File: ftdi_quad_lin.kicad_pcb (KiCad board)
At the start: 2 copper layers, 54.2 x 53 mm, 95 parts, among them J1 USB_C_Receptacle_USB2.0_16P, J2 Screw_Terminal_01x03, J3 Screw_Terminal_01x03, J4 Screw_Terminal_01x03, J5 Screw_Terminal_01x03, J6 Conn_01x10, J8 Barrel_Jack_MountingPin, U1 FT4232H, U2 TJA1029T, U3 AP2112K-3.3, U4 93CxxB, U5 TJA1029T, U6 TJA1029T, U7 TJA1029T, U8 74HC595, Y1 12Mhz

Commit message: reoredered
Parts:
- moved C1 4.00 mm to (92.2, 104.0)
- moved C3 2.99 mm to (95.8, 103.5), turned to 180 degrees
- moved R4 2.85 mm to (89.0, 102.8), turned to 180 degrees
- moved C7 1.10 mm to (92.2, 98.7)
- moved FB2 0.90 mm to (88.5, 100.2), turned to 0 degrees
- moved R3 0.25 mm to (95.8, 105.5)
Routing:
- net GND: track 148.0 -> 137.6 mm, vias 65 -> 79
- net Net-(U1-VPHY): track 17.2 -> 11.5 mm
- net Net-(J1-CC1): track 3.45 -> 6.47 mm
- net Net-(U1-OSCO): track 8.19 -> 9.53 mm
- net +3V3: track 84.4 -> 85.7 mm

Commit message: Using bus
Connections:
- net /EECLK renamed /eeprom/EECLK
- net /EECS renamed /eeprom/EECS
- net /EEDATA renamed /eeprom/EEDATA
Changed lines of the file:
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@@
 	(net 61 "unconnected-(Y1-Pad2)")
 	(net 62 "unconnected-(Y1-Pad4)")
-	(net 63 "/EECS")
-	(net 64 "/EECLK")
-	(net 65 "/EEDATA")
+	(net 63 "/eeprom/EECS")
+	(net 64 "/eeprom/EECLK")
+	(net 65 "/eeprom/EEDATA")
 	(net 66 "Net-(U8-QB)")
 	(net 67 "/PWREN")
@@
 		)
 		(property ki_fp_filters "C_*")
-		(sheetname "Root")
-		(sheetfile "ftdi_quad_lin.kicad_sch")
+		(sheetname "eeprom")
+		(sheetfile "eeprom.kicad_sch")
 		(attr smd)
 		(fp_line
@@
 		)
 		(property ki_fp_filters "DIP*W7.62mm* SOIC*3.9x9.9mm*P1.27mm* TSSOP*4.4x5mm*P0.65mm* SOIC*5.3x10.2mm*P1.27mm* SOIC*7.5x10.3mm*P1.27mm*")
-		(sheetname "Root")
-		(sheetfile "ftdi_quad_lin.kicad_sch")
+		(sheetname "leds_indication")
+		(sheetfile "leds_indication.kicad_sch")
 		(attr smd)
 		(fp_line
@@
 			(layers "F.Cu" "F.Paste" "F.Mask")
 			(roundrect_rratio 0.25)
-			(net 64 "/EECLK")
+			(net 64 "/eeprom/EECLK")
 			(pinfunction "SRCLK")
 			(pintype "input")
@@
 			(layers "F.Cu" "F.Paste" "F.Mask")
 			(roundrect_rratio 0.25)
-			(net 63 "/EECS")
+			(net 63 "/eeprom/EECS")
 			(pinfunction "RCLK")
 			(pintype "input")
@@
 			(layers "F.Cu" "F.Paste" "F.Mask")
 			(roundrect_rratio 0.25)
-			(net 65 "/EEDATA")
+			(net 65 "/eeprom/EEDATA")
 			(pinfunction "SER")
 			(pintype "input")
@@
 		)
 		(property ki_fp_filters "R_*")
-		(sheetname "Root")
-		(sheetfile "ftdi_quad_lin.kicad_sch")
+		(sheetname "eeprom")
+		(sheetfile "eeprom.kicad_sch")
 		(attr smd)
 		(fp_line
@@
 			(layers "F.Cu" "F.Paste" "F.Mask")
 			(roundrect_rratio 0.243902)
-			(net 63 "/EECS")
+			(net 63 "/eeprom/EECS")
 			(pintype "passive")
 		)
@@
 		(tags "capacitor handsolder")
 		(property "Reference" "C1"
-			(at -3.1875 0 360)
+			(at -3.1875 0 0)
 			(layer "F.SilkS")
 			(effects
@@
 		)
 		(fp_text user "${REFERENCE}"
-			(at 0 0 360)
+			(at 0 0 0)
 			(layer "F.Fab")
 			(effects
@@
 		)
 		(property ki_fp_filters "R_*")
-		(sheetname "Root")
-		(sheetfile "ftdi_quad_lin.kicad_sch")
+		(sheetname "leds_indication")
+		(sheetfile "leds_indication.kicad_sch")
 		(attr smd)
 		(fp_line
@@
 			(layers "F.Cu" "F.Paste" "F.Mask")
 			(roundrect_rratio 0.25)
-			(net 65 "/EEDATA")
+			(net 65 "/eeprom/EEDATA")
 			(pinfunction "EEDATA")
 			(pintype "bidirectional")
@@
 			(layers "F.Cu" "F.Paste" "F.Mask")
 			(roundrect_rratio 0.25)
-			(net 64 "/EECLK")
+			(net 64 "/eeprom/EECLK")
 			(pinfunction "EECLK")
 			(pintype "output")
@@
 			(layers "F.Cu" "F.Paste" "F.Mask")
 			(roundrect_rratio 0.25)
-			(net 63 "/EECS")
+			(net 63 "/eeprom/EECS")
 			(pinfunction "EECS")
 			(pintype "output")
@@
 		)
 		(property ki_fp_filters "DIP*W7.62mm* SOIC*3.9x4.9mm*")
-		(sheetname "Root")
-		(sheetfile "ftdi_quad_lin.kicad_sch")
+		(sheetname "eeprom")
+		(sheetfile "eeprom.kicad_sch")
 		(attr smd)
 		(fp_line
@@
 			(layers "F.Cu" "F.Paste" "F.Mask")
 			(roundrect_rratio 0.25)
-			(net 63 "/EECS")
+			(net 63 "/eeprom/EECS")
 			(pinfunction "CS")
 			(pintype "input")
@@
 			(layers "F.Cu" "F.Paste" "F.Mask")
 			(roundrect_rratio 0.25)
-			(net 64 "/EECLK")
+			(net 64 "/eeprom/EECLK")
 			(pinfunction "SCLK")
 			(pintype "input")
@@
 			(layers "F.Cu" "F.Paste" "F.Mask")
 			(roundrect_rratio 0.25)
-			(net 65 "/EEDATA")
+			(net 65 "/eeprom/EEDATA")
 			(pinfunction "DI")
 			(pintype "input")
@@
 		)
 		(property ki_fp_filters "C_*")
-		(sheetname "Root")
-		(sheetfile "ftdi_quad_lin.kicad_sch")
+		(sheetname "leds_indication")
+		(sheetfile "leds_indication.kicad_sch")
 		(attr smd)
 		(fp_line
@@
 		)
 		(property ki_fp_filters "R_*")
-		(sheetname "Root")
-		(sheetfile "ftdi_quad_lin.kicad_sch")
+		(sheetname "leds_indication")
+		(sheetfile "leds_indication.kicad_sch")
 		(attr smd)
 		(fp_line
@@
 		)
 		(property ki_fp_filters "R_*")
-		(sheetname "Root")
-		(sheetfile "ftdi_quad_lin.kicad_sch")
+		(sheetname "eeprom")
+		(sheetfile "eeprom.kicad_sch")
 		(attr smd)
 		(fp_line
@@
 			(layers "F.Cu" "F.Paste" "F.Mask")
 			(roundrect_rratio 0.243902)
-			(net 64 "/EECLK")
+			(net 64 "/eeprom/EECLK")
 			(pintype "passive")
 		)
@@
 		)
 		(property ki_fp_filters "R_*")
-		(sheetname "Root")
-		(sheetfile "ftdi_quad_lin.kicad_sch")
+		(sheetname "leds_indication")
+		(sheetfile "leds_indication.kicad_sch")
 		(attr smd)
 		(fp_line
@@
 			)
 		)
-		(sheetname "Root")
-		(sheetfile "ftdi_quad_lin.kicad_sch")
+		(sheetname "leds_indication")
+		(sheetfile "leds_indication.kicad_sch")
 		(attr smd)
 		(fp_line
@@
 		)
 		(property ki_fp_filters "R_*")
-		(sheetname "Root")
-		(sheetfile "ftdi_quad_lin.kicad_sch")
+		(sheetname "leds_indication")
+		(sheetfile "leds_indication.kicad_sch")
 		(attr smd)
 		(fp_line
@@
 		)
 		(property "Value" "5.1k"
-			(at 0 1.65 360)
+			(at 0 1.65 0)
 			(layer "F.Fab")
 			(effects
@@
 		)
 		(fp_text user "${REFERENCE}"
-			(at 0 0 360)
+			(at 0 0 0)
 			(layer "F.Fab")
 			(effects
@@
 		)
 		(property ki_fp_filters "R_*")
-		(sheetname "Root")
-		(sheetfile "ftdi_quad_lin.kicad_sch")
+		(sheetname "leds_indication")
+		(sheetfile "leds_indication.kicad_sch")
 		(attr smd)
 		(fp_line
@@
 		)
 		(property ki_fp_filters "R_*")
-		(sheetname "Root")
-		(sheetfile "ftdi_quad_lin.kicad_sch")
+		(sheetname "eeprom")
+		(sheetfile "eeprom.kicad_sch")
 		(attr smd)
 		(fp_line
@@
 		)
 		(property ki_fp_filters "R_*")
-		(sheetname "Root")
-		(sheetfile "ftdi_quad_lin.kicad_sch")
+		(sheetname "eeprom")
+		(sheetfile "eeprom.kicad_sch")
 		(attr smd)
 		(fp_line
@@
 			(layers "F.Cu" "F.Paste" "F.Mask")
 			(roundrect_rratio 0.243902)
-			(net 65 "/EEDATA")
+			(net 65 "/eeprom/EEDATA")
 			(pintype "passive")
 		)
@@
 		(tags "inductor handsolder")
 		(property "Reference" "FB2"
-			(at 0 -1.43 360)
+			(at 0 -1.43 0)
 			(layer "F.SilkS")
 			(effects
@@
 		)
 		(property "Value" "600R/0.5A"
-			(at -1.25 1.93 360)
+			(at -1.25 1.93 0)
 			(layer "F.Fab")
 			(effects
@@
 		)
 		(fp_text user "${REFERENCE}"
-			(at 0 0 360)
+			(at 0 0 0)
 			(layer "F.Fab")
 			(effects

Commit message: progress
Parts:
- added C30: 220n, Capacitor_SMD:C_0805_2012Metric_Pad1.18x1.45mm_HandSolder, F.Cu at (210.4, 9.20)
- added C31: 100n, Capacitor_SMD:C_0805_2012Metric_Pad1.18x1.45mm_HandSolder, F.Cu at (197.2, 10.6)
- added C32: 220n, Capacitor_SMD:C_0805_2012Metric_Pad1.18x1.45mm_HandSolder, F.Cu at (212.3, 30.8)
- added C33: 100n, Capacitor_SMD:C_0805_2012Metric_Pad1.18x1.45mm_HandSolder, F.Cu at (199.1, 32.2)
- added C34: 220n, Capacitor_SMD:C_0805_2012Metric_Pad1.18x1.45mm_HandSolder, F.Cu at (190.6, 31.1)
- added C35: 100n, Capacitor_SMD:C_0805_2012Metric_Pad1.18x1.45mm_HandSolder, F.Cu at (177.4, 32.5)
- added C36: 220n, Capacitor_SMD:C_0805_2012Metric_Pad1.18x1.45mm_HandSolder, F.Cu at (212.9, 47.6)
- added C37: 100n, Capacitor_SMD:C_0805_2012Metric_Pad1.18x1.45mm_HandSolder, F.Cu at (199.7, 49.0)
- added D11: 1N4148W, Diode_SMD:D_SOD-323_HandSoldering, F.Cu at (199.8, 13.6)
- added D12: 1N4148W, Diode_SMD:D_SOD-323_HandSoldering, F.Cu at (201.7, 35.2)
- added D13: 1N4148W, Diode_SMD:D_SOD-323_HandSoldering, F.Cu at (202.2, 52.0)
- added Q1: MMBT2222A, Package_TO_SOT_SMD:SOT-23, F.Cu at (200.1, 8.74)
- added Q10: MMBT2222A, Package_TO_SOT_SMD:SOT-23, F.Cu at (202.6, 47.1)
- added Q11: MMBT2222A, Package_TO_SOT_SMD:SOT-23, F.Cu at (209.9, 47.8)
- added Q12: MMBT2222A, Package_TO_SOT_SMD:SOT-23, F.Cu at (209.9, 51.4)
- added Q2: MMBT2222A, Package_TO_SOT_SMD:SOT-23, F.Cu at (207.4, 9.40)
- added Q3: MMBT2222A, Package_TO_SOT_SMD:SOT-23, F.Cu at (207.4, 12.9)
- added Q4: MMBT2222A, Package_TO_SOT_SMD:SOT-23, F.Cu at (201.9, 30.3)
- added Q5: MMBT2222A, Package_TO_SOT_SMD:SOT-23, F.Cu at (209.3, 31.0)
- added Q6: MMBT2222A, Package_TO_SOT_SMD:SOT-23, F.Cu at (209.3, 34.5)
- added Q7: MMBT2222A, Package_TO_SOT_SMD:SOT-23, F.Cu at (180.2, 30.6)
- added Q8: MMBT2222A, Package_TO_SOT_SMD:SOT-23, F.Cu at (187.6, 31.2)
- added Q9: MMBT2222A, Package_TO_SOT_SMD:SOT-23, F.Cu at (187.6, 34.8)
- added R26: 10k, Resistor_SMD:R_0805_2012Metric, F.Cu at (210.4, 12.9)
- added R27: 10k, Resistor_SMD:R_0805_2012Metric, F.Cu at (200.1, 11.6)
- added R28: 10k, Resistor_SMD:R_0805_2012Metric, F.Cu at (205.5, 31.4)
- added R29: 330k, Resistor_SMD:R_0805_2012Metric, F.Cu at (205.5, 33.4)
- added R30: 10k, Resistor_SMD:R_0805_2012Metric, F.Cu at (205.5, 35.4)
- added R31: 10k, Resistor_SMD:R_0805_2012Metric, F.Cu at (205.5, 29.4)
- added R32: 10k, Resistor_SMD:R_0805_2012Metric, F.Cu at (212.3, 34.5)
- added R33: 10k, Resistor_SMD:R_0805_2012Metric, F.Cu at (202.0, 33.2)
- added R34: 10k, Resistor_SMD:R_0805_2012Metric, F.Cu at (183.8, 31.6)
- added R35: 330k, Resistor_SMD:R_0805_2012Metric, F.Cu at (183.8, 33.6)
- added R36: 10k, Resistor_SMD:R_0805_2012Metric, F.Cu at (183.8, 35.6)
- added R37: 10k, Resistor_SMD:R_0805_2012Metric, F.Cu at (183.8, 29.6)
- added R38: 10k, Resistor_SMD:R_0805_2012Metric, F.Cu at (190.6, 34.7)
- added R39: 10k, Resistor_SMD:R_0805_2012Metric, F.Cu at (180.3, 33.5)
- added R40: 10k, Resistor_SMD:R_0805_2012Metric, F.Cu at (206.1, 48.2)
- added R41: 330k, Resistor_SMD:R_0805_2012Metric, F.Cu at (206.1, 50.2)
- added R42: 10k, Resistor_SMD:R_0805_2012Metric, F.Cu at (206.1, 52.2)
- added R43: 10k, Resistor_SMD:R_0805_2012Metric, F.Cu at (206.1, 46.2)
- added R44: 10k, Resistor_SMD:R_0805_2012Metric, F.Cu at (212.9, 51.3)
- added R45: 10k, Resistor_SMD:R_0805_2012Metric, F.Cu at (202.6, 50.0)
- D10: value ~ -> 1N4148W; footprint ftdi_quad_lin:1296.3004 -> Diode_SMD:D_SOD-323_HandSoldering
- D9: footprint ftdi_quad_lin:1296.3004 -> ftdi_quad_lin:1276.2004
- R17, R19, R20: value 330R -> 1k
- R22, R24, R25: value 2.4k -> 10k
- R23: value 2.4k -> 330k
- moved R22 115.8 mm to (203.6, 9.80), turned to 180 degrees
- moved R23 113.0 mm to (203.6, 11.8), turned to 180 degrees
- moved R25 112.3 mm to (203.6, 7.80), turned to 180 degrees
- moved R24 110.4 mm to (203.6, 13.8), turned to 180 degrees
- moved D10 83.4 mm to (179.9, 35.5), turned to 180 degrees
- moved D9 21.3 mm to (107.4, 57.6)
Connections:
- net Net-(D3-K) renamed /VBAT1
- net Net-(D5-K) renamed /VBAT2
- net Net-(D7-K) renamed /VBAT3
- C17 pad 1: Net-(D1-K) -> /VBAT0
- D1 pad 1: Net-(D1-K) -> /VBAT0
- D1 pad 2: /LIN 0/VBAT -> Net-(D1-A)
- D10 pad 1: GND -> Net-(D10-K)
- D10 pad 2: Net-(D10-Pad2) -> Net-(D10-A)
- D3 pad 2: /LIN 1/VBAT -> Net-(D3-A)
- D5 pad 2: /LIN 2/VBAT -> Net-(D5-A)
- D7 pad 2: /LIN 3/VBAT -> Net-(D7-A)
- D9 pad 1: GND -> +5V
- D9 pad 3: GND -> +5V
- D9 pad 5: GND -> +5V
- D9 pad 7: GND -> +5V
- J2 pad 1: /LIN 0/VBAT -> Net-(D1-A)
- J3 pad 1: /LIN 1/VBAT -> Net-(D3-A)
- J4 pad 1: /LIN 2/VBAT -> Net-(D5-A)
- J5 pad 1: /LIN 3/VBAT -> Net-(D7-A)
- JP1 pad 1: Net-(D1-K) -> /VBAT0
- JP5 pad 2: /LIN 0/VBAT -> Net-(D1-A)
- JP6 pad 2: /LIN 1/VBAT -> Net-(D3-A)
- JP7 pad 2: /LIN 2/VBAT -> Net-(D5-A)
- JP8 pad 2: /LIN 3/VBAT -> Net-(D7-A)
- R17 pad 2: Net-(U8-QB) -> /leds_indication/led_indication_0/LED
- R19 pad 2: Net-(U8-QD) -> /leds_indication/led_indication_1/LED
- R20 pad 2: Net-(U8-QF) -> /leds_indication/led_indication_2/LED
- R21 pad 2: Net-(U8-QH) -> /leds_indication/led_indication_3/LED
- R22 pad 1: Net-(D10-Pad2) -> Net-(Q2-C)
- R22 pad 2: /LIN 0/VBAT -> /VBAT0
- R23 pad 1: Net-(D10-Pad4) -> Net-(Q3-B)
- R23 pad 2: /LIN 1/VBAT -> /VBAT0
- R24 pad 1: Net-(D10-Pad6) -> Net-(Q3-C)
- R24 pad 2: /LIN 2/VBAT -> /VBAT0
- R25 pad 1: Net-(D10-Pad8) -> Net-(Q2-C)
- R25 pad 2: /LIN 3/VBAT -> Net-(Q1-B)
- U2 pad 7: Net-(D1-K) -> /VBAT0
- U8 pad 1: Net-(U8-QB) -> /leds_indication/led_indication_0/INDICATION
- U8 pad 3: Net-(U8-QD) -> /leds_indication/led_indication_1/INDICATION
- U8 pad 5: Net-(U8-QF) -> /leds_indication/led_indication_2/INDICATION
- U8 pad 7: Net-(U8-QH) -> /leds_indication/led_indication_3/INDICATION
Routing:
- net /LIN 2/VBAT: track 81.2 -> 0.00 mm
- net /LIN 0/VBAT: track 69.7 -> 0.00 mm, vias 1 -> 0
- net Net-(D1-A): track 0.00 -> 65.9 mm
- net /LIN 3/VBAT: track 63.0 -> 0.00 mm
- net /LIN 1/VBAT: track 59.7 -> 0.00 mm, vias 1 -> 0
- net Net-(D3-A): track 0.00 -> 57.8 mm
- net Net-(D5-A): track 0.00 -> 57.6 mm
- net Net-(D7-A): track 0.00 -> 49.8 mm
- net Net-(U8-QH): track 32.2 -> 0.00 mm
- net Net-(U8-QB): track 30.3 -> 0.00 mm
- net Net-(U8-QD): track 30.0 -> 0.00 mm
- net Net-(U8-QF): track 28.8 -> 0.00 mm
- net Net-(D13-K): track 0.00 -> 22.5 mm
- net Net-(D11-K): track 0.00 -> 22.5 mm
- net Net-(D10-K): track 0.00 -> 22.5 mm
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
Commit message: progress
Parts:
- removed D9: ~, ftdi_quad_lin:1276.2004
- added D14: LED, ftdi_quad_lin:1216.1002, F.Cu at (111.8, 54.2)
- added D15: LED, ftdi_quad_lin:1216.1002, F.Cu at (111.5, 73.0)
- added D16: LED, ftdi_quad_lin:1216.1002, F.Cu at (123.7, 85.0)
- added D17: LED, ftdi_quad_lin:1216.1002, F.Cu at (120.6, 104.4)
- added REF**: DSUB-9_Female_Vertical_P2.77x2.84mm, Connector_Dsub:DSUB-9_Female_Vertical_P2.77x2.84mm, F.Cu at (157.6, 71.4)
- added REF**: DSUB-9_Female_Vertical_P2.77x2.84mm, Connector_Dsub:DSUB-9_Female_Vertical_P2.77x2.84mm, F.Cu at (157.6, 90.0)
- added REF**: DSUB-9_Female_Vertical_P2.77x2.84mm, Connector_Dsub:DSUB-9_Female_Vertical_P2.77x2.84mm, F.Cu at (157.6, 52.8)
- added REF**: DSUB-9_Female_Vertical_P2.77x2.84mm, Connector_Dsub:DSUB-9_Female_Vertical_P2.77x2.84mm, F.Cu at (157.6, 108.6)
- moved JP5 34.1 mm to (96.5, 44.1), turned to -90 degrees
- moved JP6 32.2 mm to (99.0, 44.1), turned to -90 degrees
- moved R17 31.7 mm to (120.6, 103.0)
- moved JP7 30.6 mm to (101.5, 44.1), turned to -90 degrees
- moved JP8 29.2 mm to (104.0, 44.1), turned to -90 degrees
- moved H2 26.6 mm to (84.8, 45.6)
- moved H1 26.3 mm to (131.8, 46.0)
- moved C20 25.8 mm to (124.5, 57.3)
- moved C24 25.8 mm to (121.5, 58.0)
- moved D7 25.8 mm to (124.5, 53.3)
- moved D8 25.8 mm to (126.5, 53.3)
- moved JP4 25.8 mm to (123.5, 50.0)
- moved R15 25.8 mm to (117.3, 50.2)
- moved R16 25.8 mm to (126.5, 57.3)
- moved U7 25.8 mm to (119.4, 54.1)
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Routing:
- net GND: track 119.2 -> 60.9 mm, vias 76 -> 0
- net Net-(D1-A): track 65.9 -> 8.76 mm
- net Net-(D5-A): track 57.6 -> 8.09 mm
- net Net-(D3-A): track 57.8 -> 8.54 mm
- net Net-(D7-A): track 49.8 -> 8.36 mm
- net +5V: track 218.1 -> 188.8 mm, vias 3 -> 2
- net /LIN1_RXD: track 33.3 -> 7.90 mm, vias 2 -> 0
- net /LIN1_TXD: track 29.9 -> 6.04 mm, vias 2 -> 0
- net /LIN3_TXD: track 41.6 -> 17.9 mm, vias 2 -> 1
- net /LIN0_RXD: track 31.5 -> 7.86 mm, vias 2 -> 0
- net /LIN3_RXD: track 57.6 -> 34.5 mm, vias 2 -> 1
- net /LIN2_RXD: track 37.6 -> 14.7 mm, vias 2 -> 1
- net /LIN2_TXD: track 30.9 -> 12.2 mm, vias 3 -> 2
- net /LIN0_TXD: track 26.0 -> 7.40 mm
- net +3V3: track 85.7 -> 68.8 mm, vias 4 -> 3
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- removed copper zone on B.Cu, net GND
- removed copper zone on F.Cu, net GND
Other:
- board size 54.2 x 53 mm -> 55 x 80 mm
- board text removed: "data"
- board text removed: "power"

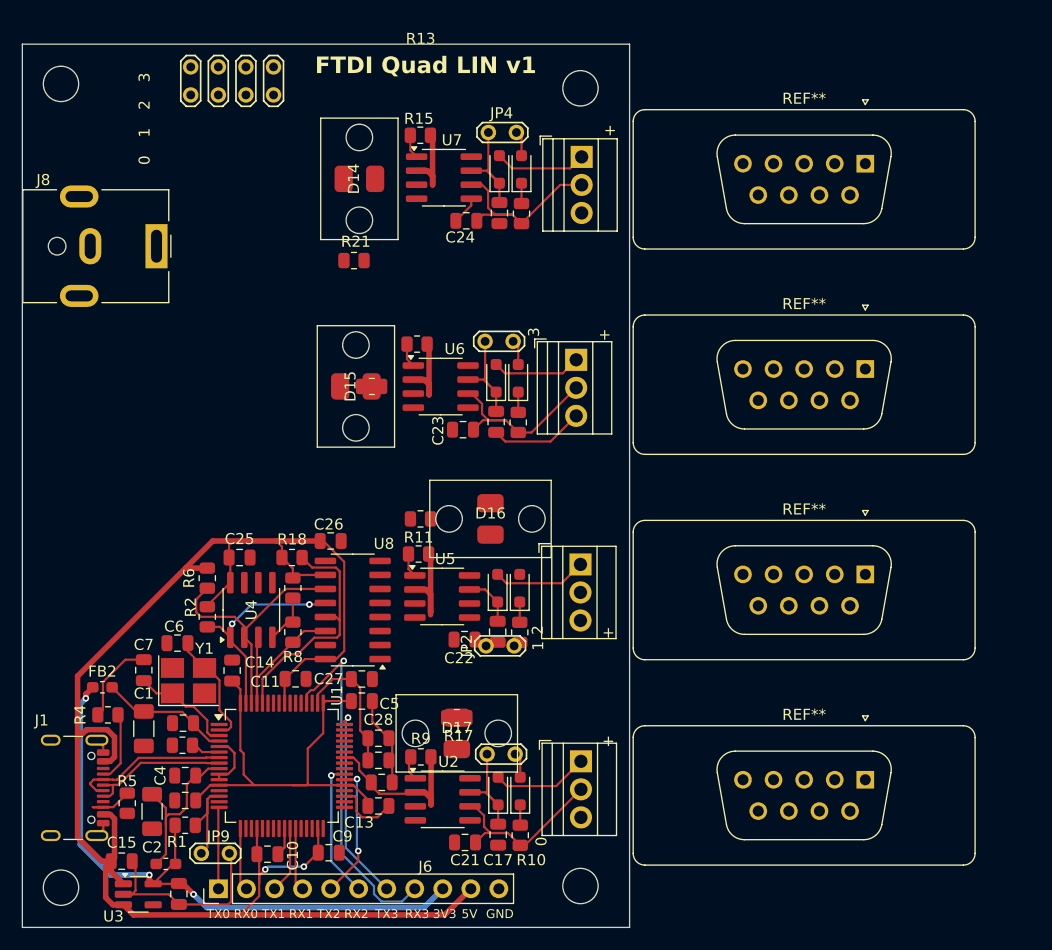
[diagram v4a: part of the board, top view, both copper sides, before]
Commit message: new connectors
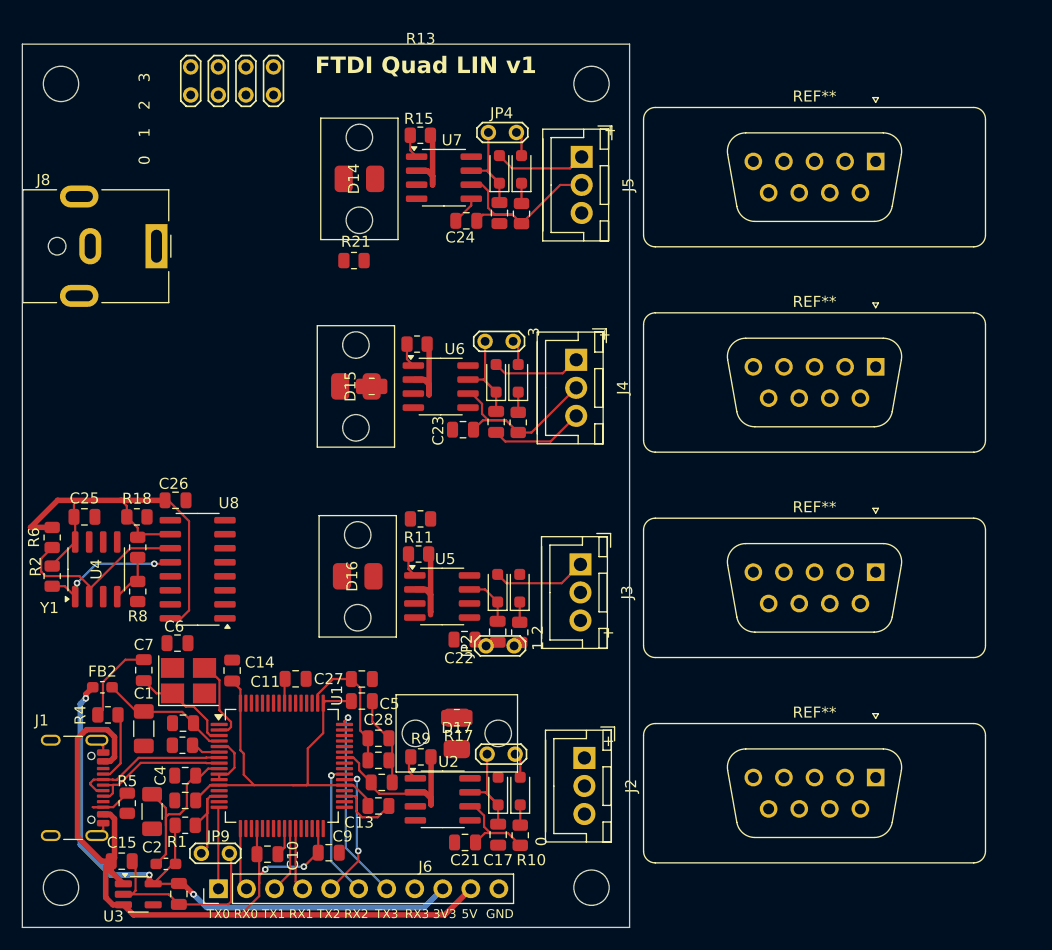
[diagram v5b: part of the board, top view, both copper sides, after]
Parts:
- removed the REF** at (157.6, 71.4)
- removed the REF** at (157.6, 90.0)
- removed the REF** at (157.6, 52.8)
- removed the REF** at (157.6, 108.6)
- added REF**: DSUB-9_Female_Vertical_P2.77x2.84mm, Connector_Dsub:DSUB-9_Female_Vertical_P2.77x2.84mm, F.Cu at (158.5, 108.4)
- added REF**: DSUB-9_Female_Vertical_P2.77x2.84mm, Connector_Dsub:DSUB-9_Female_Vertical_P2.77x2.84mm, F.Cu at (158.5, 52.6)
- added REF**: DSUB-9_Female_Vertical_P2.77x2.84mm, Connector_Dsub:DSUB-9_Female_Vertical_P2.77x2.84mm, F.Cu at (158.5, 71.2)
- added REF**: DSUB-9_Female_Vertical_P2.77x2.84mm, Connector_Dsub:DSUB-9_Female_Vertical_P2.77x2.84mm, F.Cu at (158.5, 89.8)
- J2, J3, J4, J5: footprint TerminalBlock:TerminalBlock_Xinya_XY308-2.54-3P_1x03_P2.54mm_Horizontal -> ftdi_quad_lin:lin_connector
- moved C25 14.5 mm to (86.9, 84.8)
- moved C26 14.5 mm to (95.1, 83.3)
- moved R18 14.5 mm to (91.6, 84.8)
- moved R2 14.5 mm to (84.0, 90.2)
- moved R6 14.5 mm to (84.0, 86.7)
- moved R7 14.5 mm to (91.7, 87.6)
- moved R8 14.5 mm to (91.7, 91.6)
- moved U4 14.5 mm to (87.9, 89.6)
- moved U8 14.5 mm to (97.1, 89.6)
- moved D16 13.1 mm to (111.6, 90.2), turned to 90 degrees
- moved H1 1.08 mm to (132.8, 45.6)
- moved H4 1.01 mm to (132.8, 118.4)
- moved J2 0.44 mm to (132.2, 106.7)
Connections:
- D14 pad 1: +5V -> Net-(D14-K)
- D14 pad 2: Net-(D14-A) -> +5V
- D15 pad 1: +5V -> Net-(D15-K)
- D15 pad 2: Net-(D15-A) -> +5V
- D16 pad 1: +5V -> Net-(D16-K)
- D16 pad 2: Net-(D16-A) -> +5V
- D17 pad 1: +5V -> Net-(D17-K)
- D17 pad 2: Net-(D17-A) -> +5V
- R17 pad 1: Net-(D14-A) -> Net-(D14-K)
- R19 pad 1: Net-(D15-A) -> Net-(D15-K)
- R20 pad 1: Net-(D16-A) -> Net-(D16-K)
- R21 pad 1: Net-(D17-A) -> Net-(D17-K)
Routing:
- net /LIN3_RXD: track 34.5 -> 2.18 mm, vias 1 -> 0
- net +5V: track 188.8 -> 165.0 mm
- net /PWREN: track 21.9 -> 0.00 mm
- net /eeprom/EEDATA: track 16.1 -> 0.00 mm
- net Net-(D1-A): track 8.76 -> 0.00 mm
- net /LIN 0/LIN: track 16.6 -> 9.46 mm
- net /eeprom/EECLK: track 23.6 -> 17.3 mm
- net /eeprom/EECS: track 19.0 -> 12.8 mm
- net Net-(U1-OSCI): track 10.3 -> 7.43 mm
